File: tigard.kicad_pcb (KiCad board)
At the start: 4 copper layers, 46 x 46 mm, 92 parts, among them J1 USB_C_Receptacle_USB2.0, J2 JTAG, J3 UART, J4 SPI, J5 CORTEX, J6 LA, J7 I2C, Q1 BSH103, SW1 TARGET, SW2 MODE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

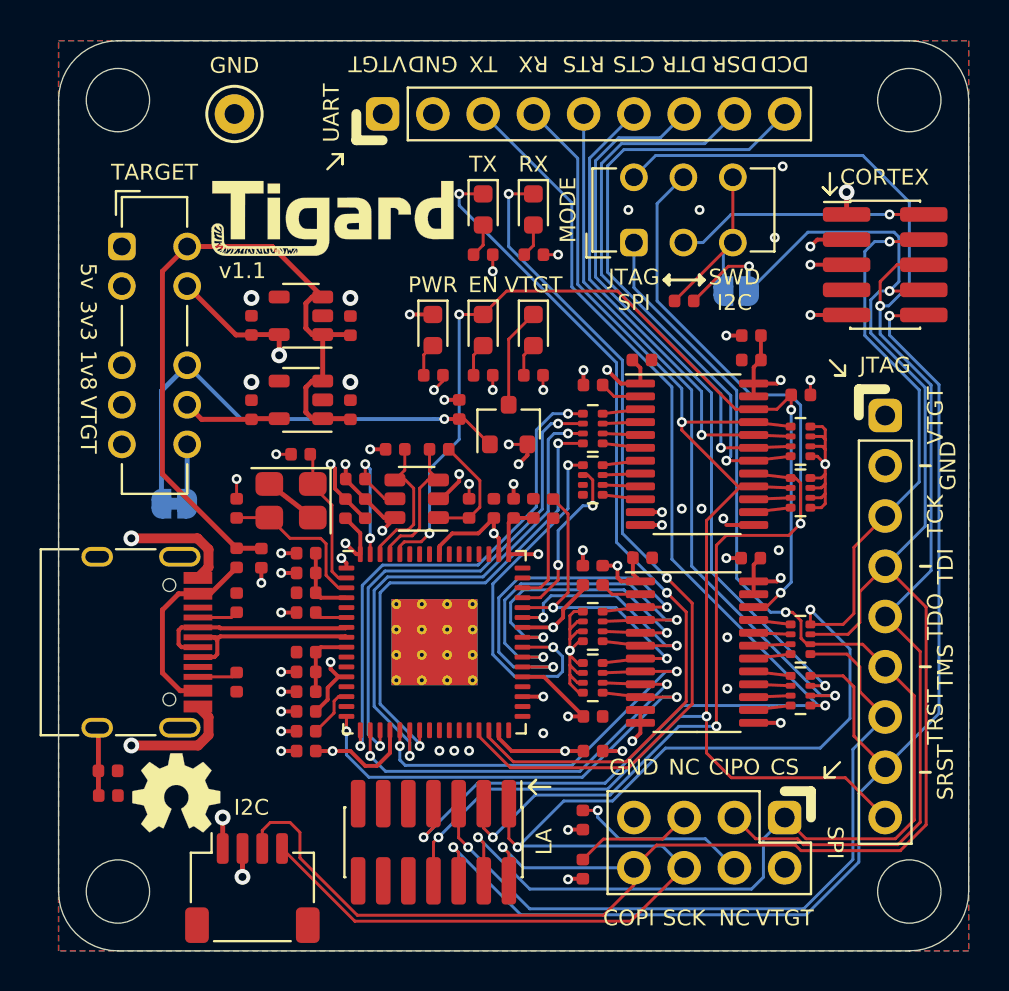
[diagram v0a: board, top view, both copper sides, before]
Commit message: adding test jig features
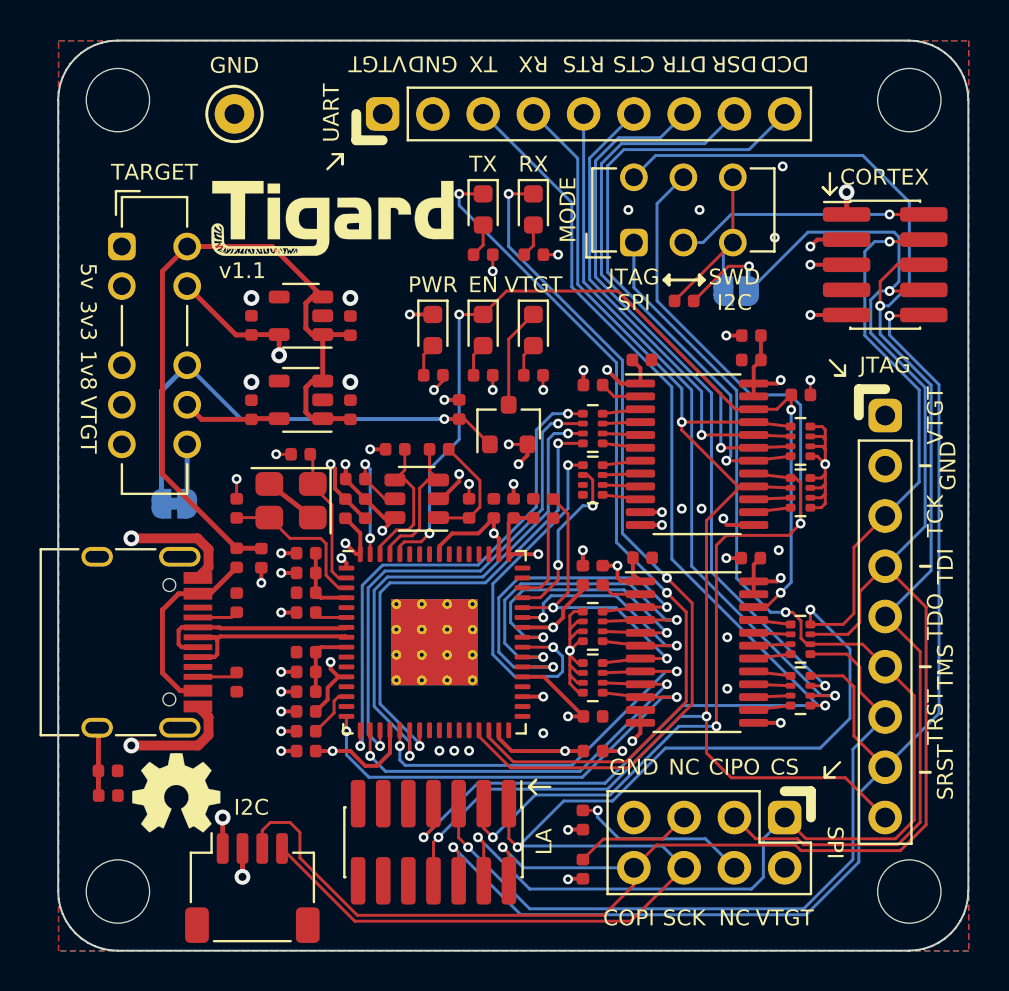
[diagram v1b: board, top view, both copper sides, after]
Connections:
- net /~ENABLE renamed /~{ENABLE}
- net /~UART_CTS renamed /~{UART_CTS}
- net /~UART_DCD renamed /~{UART_DCD}
- net /~UART_DSR renamed /~{UART_DSR}
- net /~UART_DTR renamed /~{UART_DTR}
- net /~UART_RTS renamed /~{UART_RTS}
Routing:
- added copper zone on In2.Cu, net +3V3
- added copper zone on In1.Cu, net GND
- removed copper zone on PWR, net +3V3
- removed copper zone on GND, net GND
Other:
- outline, holes or cut-outs redrawn
- net class Default removed
